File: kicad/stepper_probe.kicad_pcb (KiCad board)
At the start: 2 copper layers, 33 x 42 mm, 49 parts, among them J1 Conn_01x04_Male, J2 Conn_01x04_Male, J3 BAT, J4 Serial Port, J5 SWD, J6 Reset header, M1 Motor, Q1 PJA3439, SW1 SW_Push, U1 CC6920BSO-5A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

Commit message: Minor PCB tweaks, moved LEDs, added pin 1 marks, added zenner silk screen.  No electrical or bom change.
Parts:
- D4: footprint Diode_SMD:D_MiniMELF -> stepper_probe:D_MiniMELF_zenner
- moved R7 1.37 mm to (168.4, 76.9)
- moved D1 1.32 mm to (164.6, 76.9)
- moved R6 0.62 mm to (165.5, 76.9)
- moved D2 0.56 mm to (167.4, 76.9)
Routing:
- net GND: track 82.7 -> 84.1 mm, vias 19 -> 18
- net /LED2: track 9.17 -> 10.5 mm
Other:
- board text added: "V0.1.3.1"
- board text removed: "V0.1.3"

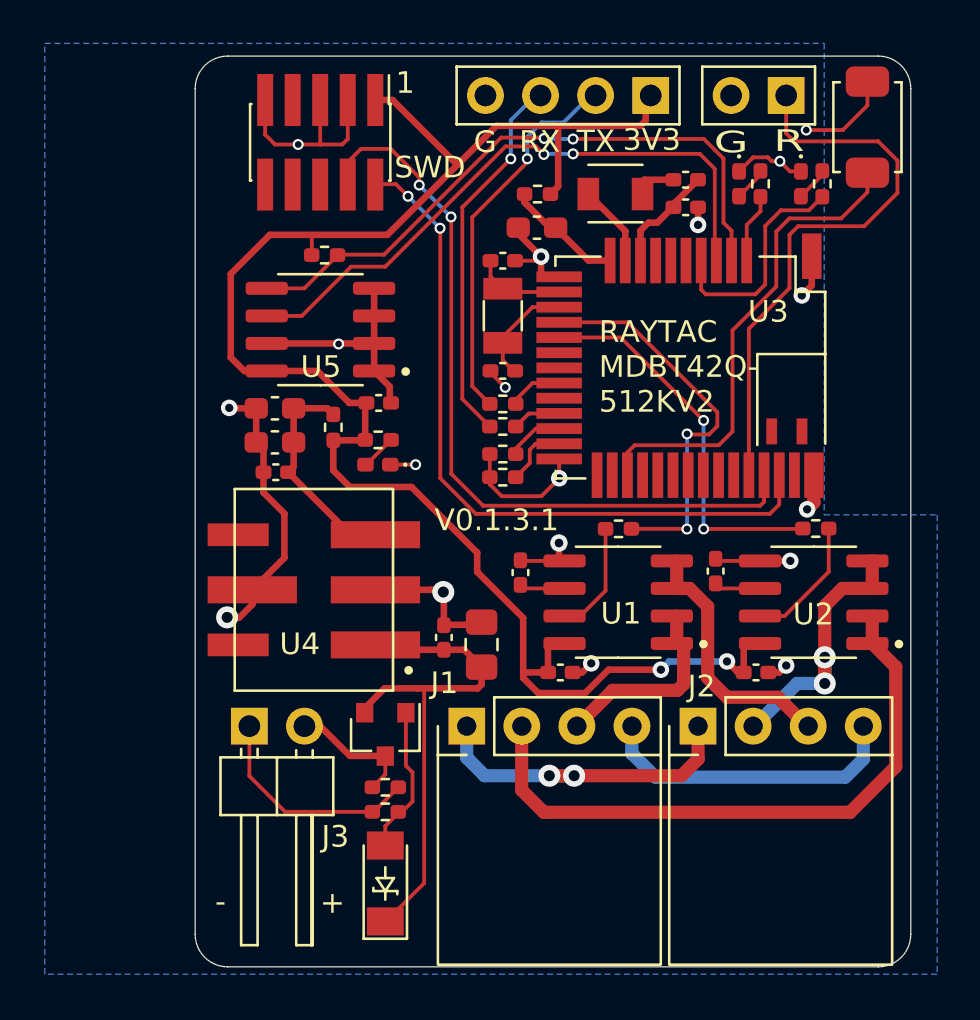
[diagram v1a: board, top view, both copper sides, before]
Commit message: Now using average for zero calibration. Also updated README and Kicad.
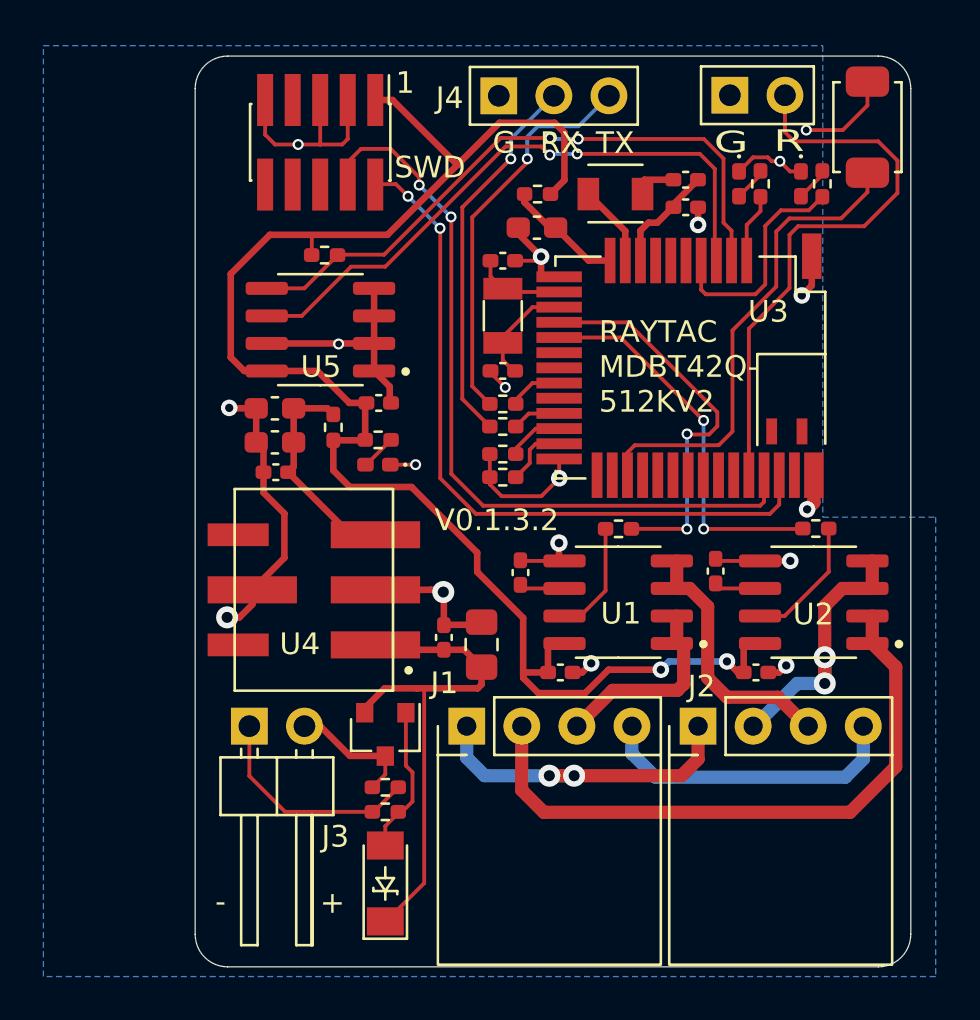
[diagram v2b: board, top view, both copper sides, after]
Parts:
- J4: value Serial Port -> Conn_01x03_Male; footprint stepper_probe:PinHeader_1x04_P2.54mm_Vertical -> stepper_probe:PinHeader_1x03_P2.54mm_Vertical
- moved J4 7.01 mm to (153.5, 72.9), turned to 90 degrees
- moved J6 2.60 mm to (164.1, 72.9), turned to 90 degrees
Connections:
- J4 pad 1: +3V3 -> GND
- J6 pad 1: /RESET -> GND
- J6 pad 2: GND -> /RESET
- R8 pad 1: Net-(J4-Pad2) -> Net-(J4-Pad3)
- R9 pad 1: Net-(J4-Pad3) -> Net-(J4-Pad2)
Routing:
- net +3V3: track 79.2 -> 74.2 mm
- net Net-(J4-Pad3): track 17.1 -> 18.3 mm
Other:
- board text added: "V0.1.3.2"
- board text removed: "3V3"
- board text removed: "V0.1.3.1"

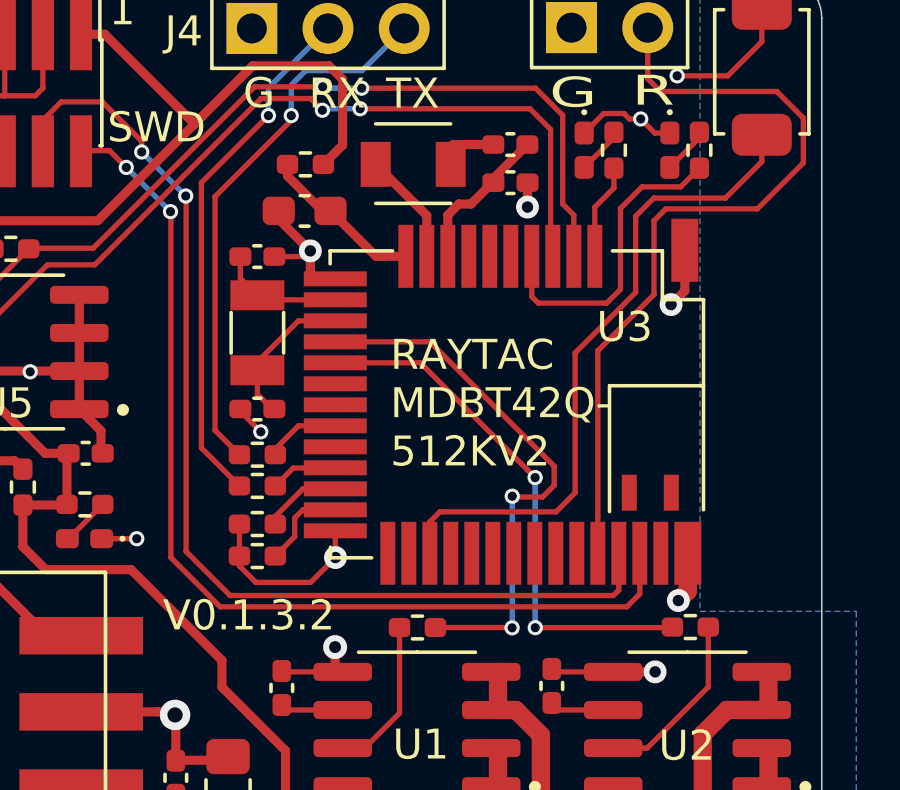
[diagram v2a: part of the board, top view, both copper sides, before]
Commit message: Fixed nrf52 footprint.
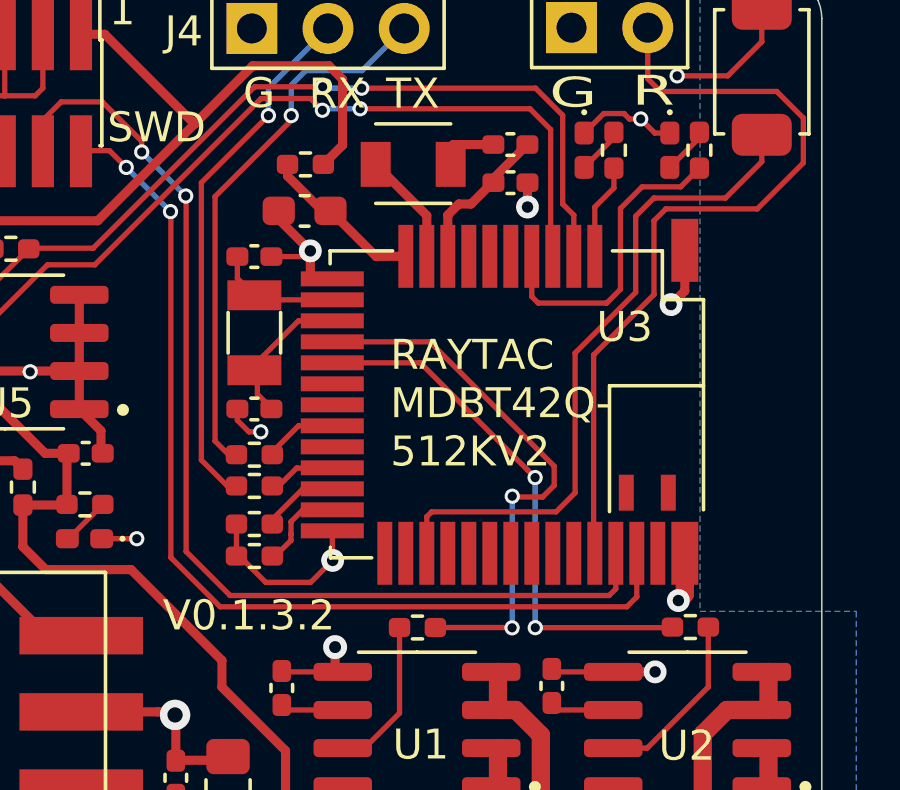
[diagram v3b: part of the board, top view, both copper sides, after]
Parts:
- moved C3 0.10 mm to (153.6, 80.5)
- moved C5 0.10 mm to (153.6, 85.6)
- moved R11 0.10 mm to (153.6, 89.4)
- moved R12 0.10 mm to (153.6, 90.5)
- moved R8 0.10 mm to (153.6, 87.1)
- moved R9 0.10 mm to (153.6, 88.1)
- moved Y1 0.10 mm to (153.6, 83.0)

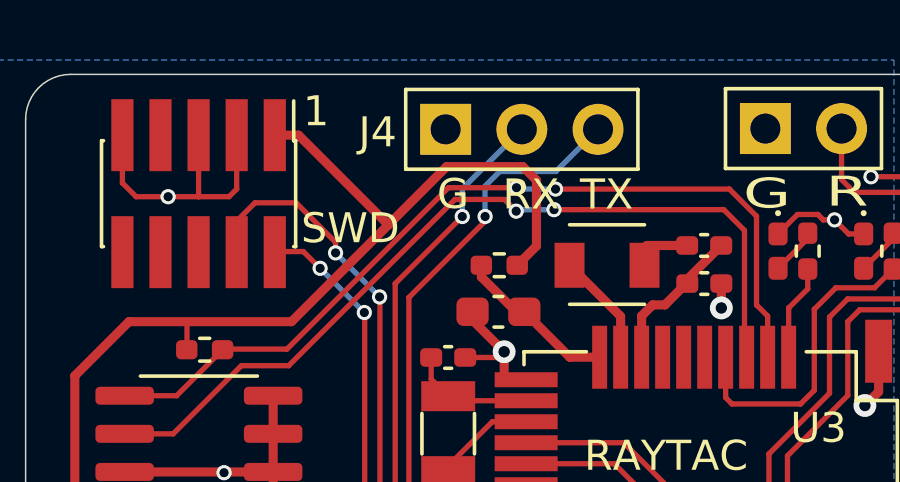
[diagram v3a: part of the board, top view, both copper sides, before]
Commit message: Added 3 pins header to the JLCPCB BOM.
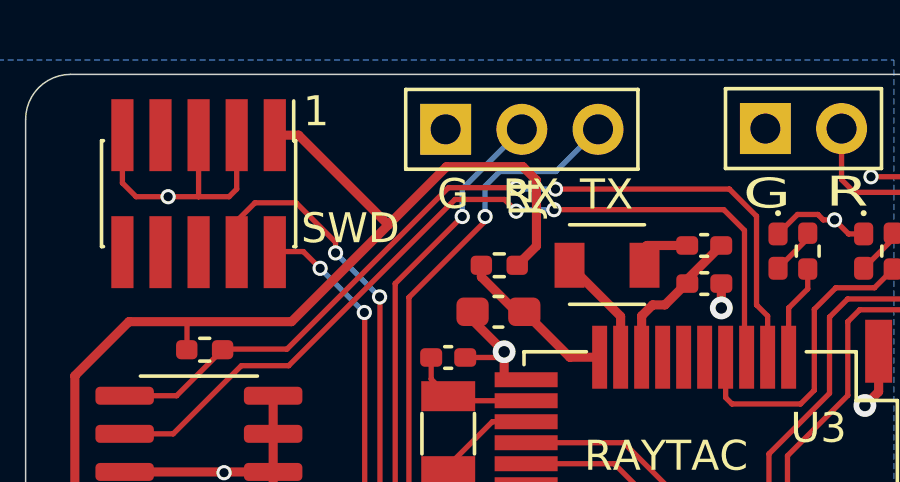
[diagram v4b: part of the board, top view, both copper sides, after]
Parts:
- moved J4 2.54 mm to (156.0, 72.9), turned to 180 degrees
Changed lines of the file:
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@@
   )
   (module stepper_probe:PinHeader_1x03_P2.54mm_Vertical (layer F.Cu)
-    (at 153.47188 72.88784 90)
+    (at 156.01188 72.88784 180)
     (descr "Through hole straight pin header, 1x03, 2.54mm pitch, single row")
     (tags "Through hole pin header THT 1x03 2.54mm single row")
-    (fp_text reference J4 (at -0.1016 -2.26568 180) (layer F.SilkS)
+    (attr smd)
+    (fp_text reference J4 (at -0.1016 -2.26568 270) (layer F.SilkS)
       (effects (font (size 1 1) (thickness 0.15)))
     )
-    (fp_text value Conn_01x03_Male (at 0 7.41 90) (layer F.Fab)
+    (fp_text value Conn_01x03_Male (at 0 7.41) (layer F.Fab)
       (effects (font (size 1 1) (thickness 0.15)))
     )
-    (fp_text user %R (at 0 2.54) (layer F.Fab)
+    (fp_text user %R (at 0 2.54 90) (layer F.Fab)
       (effects (font (size 1 1) (thickness 0.15)))
     )
-    (fp_line (start -0.635 -1.27) (end 1.27 -1.27) (layer F.Fab) (width 0.1))
-    (fp_line (start 1.27 -1.27) (end 1.27 6.35) (layer F.Fab) (width 0.1))
-    (fp_line (start 1.27 6.35) (end -1.27 6.35) (layer F.Fab) (width 0.1))
-    (fp_line (start -1.27 6.35) (end -1.27 -0.635) (layer F.Fab) (width 0.1))
-    (fp_line (start -1.27 -0.635) (end -0.635 -1.27) (layer F.Fab) (width 0.1))
-    (fp_line (start -1.33 6.41) (end 1.33 6.41) (layer F.SilkS) (width 0.12))
-    (fp_line (start -1.33 -1.33) (end -1.33 6.41) (layer F.SilkS) (width 0.12))
-    (fp_line (start 1.33 -1.33) (end 1.33 6.41) (layer F.SilkS) (width 0.12))
-    (fp_line (start -1.33 -1.33) (end 1.33 -1.33) (layer F.SilkS) (width 0.12))
-    (fp_line (start -1.8 -1.8) (end -1.8 6.85) (layer F.CrtYd) (width 0.05))
-    (fp_line (start -1.8 6.85) (end 1.8 6.85) (layer F.CrtYd) (width 0.05))
-    (fp_line (start 1.8 6.85) (end 1.8 -1.8) (layer F.CrtYd) (width 0.05))
-    (fp_line (start 1.8 -1.8) (end -1.8 -1.8) (layer F.CrtYd) (width 0.05))
-    (pad 3 thru_hole oval (at 0 5.08 90) (size 1.7 1.7) (drill 1) (layers *.Cu *.Mask)
+    (fp_line (start 3.81 -0.635) (end 3.81 1.27) (layer F.Fab) (width 0.1))
+    (fp_line (start 3.81 1.27) (end -3.81 1.27) (layer F.Fab) (width 0.1))
+    (fp_line (start -3.81 1.27) (end -3.81 -1.27) (layer F.Fab) (width 0.1))
+    (fp_line (start -3.81 -1.27) (end 3.175 -1.27) (layer F.Fab) (width 0.1))
+    (fp_line (start 3.175 -1.27) (end 3.81 -0.635) (layer F.Fab) (width 0.1))
+    (fp_line (start -3.87 -1.33) (end -3.87 1.33) (layer F.SilkS) (width 0.12))
+    (fp_line (start 3.87 -1.33) (end -3.87 -1.33) (layer F.SilkS) (width 0.12))
+    (fp_line (start 3.87 1.33) (end -3.87 1.33) (layer F.SilkS) (width 0.12))
+    (fp_line (start 3.87 -1.33) (end 3.87 1.33) (layer F.SilkS) (width 0.12))
+    (fp_line (start 4.34 -1.8) (end -4.31 -1.8) (layer F.CrtYd) (width 0.05))
+    (fp_line (start -4.31 -1.8) (end -4.31 1.8) (layer F.CrtYd) (width 0.05))
+    (fp_line (start -4.31 1.8) (end 4.34 1.8) (layer F.CrtYd) (width 0.05))
+    (fp_line (start 4.34 1.8) (end 4.34 -1.8) (layer F.CrtYd) (width 0.05))
+    (pad 3 thru_hole oval (at -2.54 0 180) (size 1.7 1.7) (drill 1) (layers *.Cu *.Mask)
       (net 12 "Net-(J4-Pad3)"))
-    (pad 2 thru_hole oval (at 0 2.54 90) (size 1.7 1.7) (drill 1) (layers *.Cu *.Mask)
+    (pad 2 thru_hole oval (at 0 0 180) (size 1.7 1.7) (drill 1) (layers *.Cu *.Mask)
       (net 13 "Net-(J4-Pad2)"))
-    (pad 1 thru_hole rect (at 0 0 90) (size 1.7 1.7) (drill 1) (layers *.Cu *.Mask)
+    (pad 1 thru_hole rect (at 2.54 0 180) (size 1.7 1.7) (drill 1) (layers *.Cu *.Mask)
       (net 36 GND))
     (model ${KISYS3DMOD}/Connector_PinHeader_2.54mm.3dshapes/PinHeader_1x03_P2.54mm_Vertical.wrl
       (at (xyz 0 0 0))
       (scale (xyz 1 1 1))
-      (rotate (xyz 0 0 0))
+      (rotate (xyz 0 0 90))
     )
   )

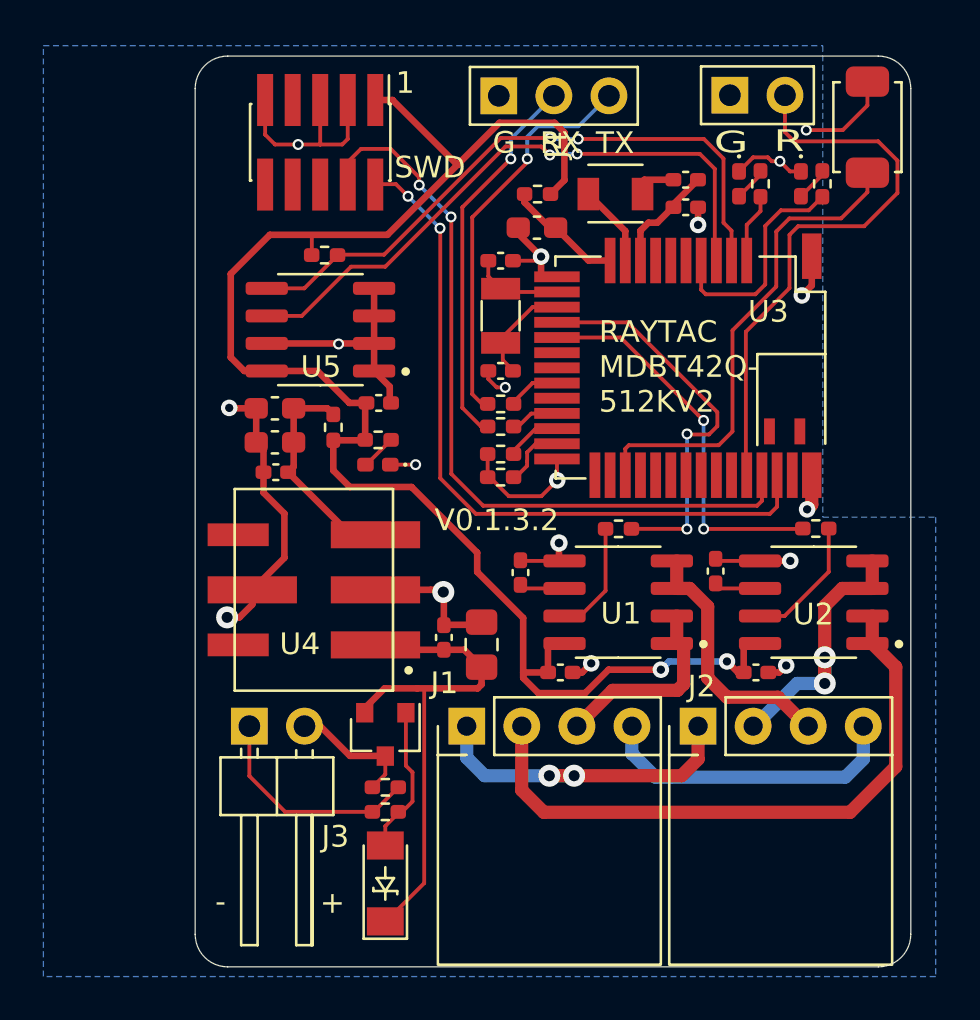
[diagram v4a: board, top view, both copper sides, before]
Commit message: Upgraded to kicad 6
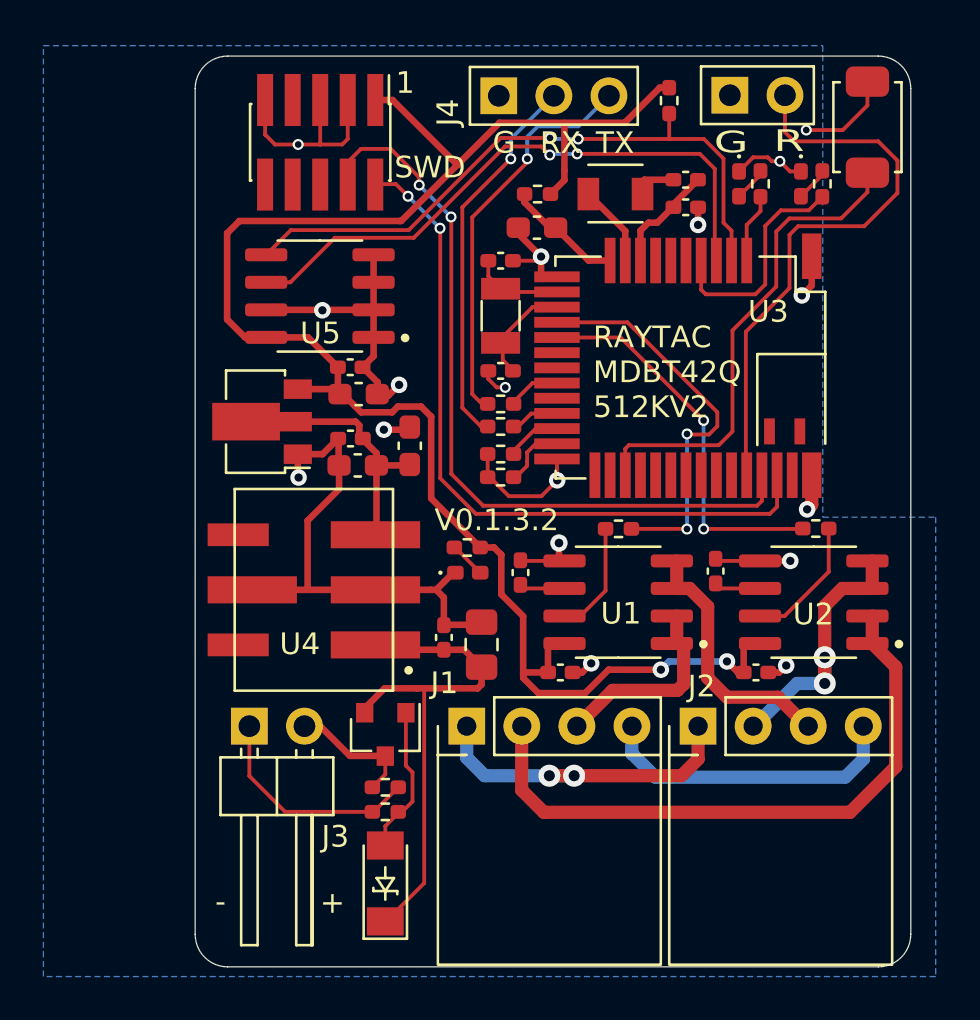
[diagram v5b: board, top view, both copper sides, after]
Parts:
- removed R14: 0R, stepper_probe:R_0402_1005Metric_Pad0.72x0.64mm_HandSolder
- added C15: 10u, stepper_probe:C_0603_1608Metric_Pad1.08x0.95mm_HandSolder, F.Cu at (149.4, 89.0)
- added U6: HT75xx-1-SOT89, Package_TO_SOT_SMD:SOT-89-3, F.Cu at (142.6, 87.9)
- moved R10 17.4 mm to (161.3, 73.1), turned to 90 degrees
- moved D3 6.48 mm to (152.0, 94.9), turned to 0 degrees
- moved R5 6.44 mm to (152.0, 93.7), turned to 0 degrees
- moved C10 4.64 mm to (147.0, 89.9)
- moved C11 4.46 mm to (147.0, 86.6), turned to 0 degrees
- moved C9 3.78 mm to (146.6, 88.7)
- moved C12 2.11 mm to (146.6, 85.4)
- moved U5 1.55 mm to (145.2, 82.1)
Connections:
- C11 pad 1: Net-(C10-Pad1) -> +3V3
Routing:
- net GND: track 84.2 -> 91.4 mm, vias 18 -> 17
- net +3V3: track 74.2 -> 80.2 mm
- net /SCL: track 28.6 -> 28.0 mm
- net /SDA: track 29.2 -> 29.7 mm
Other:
- net class Default removed
- board text added: "RAYTAC MDBT42Q 512KV2"
- board text removed: "RAYTAC MDBT42Q- 512KV2"
